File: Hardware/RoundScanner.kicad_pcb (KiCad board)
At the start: 2 copper layers, 50.1 x 50.1 mm, 87 parts, among them J1 I2C Debug, J2 Screen, J3 SPI Debug, SW1 TRIGGER, SW2 RESET, U1 OPA2376xxD, U2 ADS1256IDBT, U3 LM285D-2.5, U4 AMS1117-3.3, U5 TLC59208FIPWR, U6 ESP32-DevKitC, Y1 8MHz

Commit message: Version 0.1
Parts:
- removed B1: Button, Connector_JST:JST_SH_BM04B-SRSS-TB_1x04-1MP_P1.00mm_Vertical
- removed CH1: Power, Connector_JST:JST_XH_B2B-XH-A_1x02_P2.50mm_Vertical
- removed D12: WS2812B, LED_SMD:LED_WS2812B_PLCC4_5.0x5.0mm_P3.2mm
- removed FB1: FerriteBead, Resistor_SMD:R_0805_2012Metric_Pad1.20x1.40mm_HandSolder
- removed J3: SPI Debug, Connector_JST:JST_XH_B4B-XH-A_1x04_P2.50mm_Vertical
- removed JP1: SolderJumper_2_Open, Jumper:SolderJumper-2_P1.3mm_Open_TrianglePad1.0x1.5mm
- removed JP2, JP3: SolderJumper_3_Open, Jumper:SolderJumper-3_P2.0mm_Open_TrianglePad1.0x1.5mm_NumberLabels
- removed R13: 0, Resistor_SMD:R_0805_2012Metric_Pad1.20x1.40mm_HandSolder
- removed R14, R15: 100, Resistor_SMD:R_0805_2012Metric_Pad1.20x1.40mm_HandSolder
- removed R19: 10k, Resistor_SMD:R_0805_2012Metric_Pad1.20x1.40mm_HandSolder
- removed SW1: TRIGGER, Button_Switch_THT:SW_PUSH_6mm
- removed SW2: RESET, Button_Switch_THT:SW_PUSH_6mm
- removed TP0: Test_GND, TestPoint:TestPoint_Pad_D1.5mm
- removed TP1: Test_5V, TestPoint:TestPoint_Pad_D1.5mm
- removed TP52: TestPoint_Small, TestPoint:TestPoint_Pad_D1.0mm
- removed Y1: 8MHz, Crystal:Crystal_SMD_3225-4Pin_3.2x2.5mm_HandSoldering
- added L1: INDUCTOR, Inductor_SMD:L_0603_1608Metric, F.Cu at (106.0, 119.1)
- added Q1: BSS138DW-7-F, BSS138DW-7-F-A:Diodes_Inc._-_BSS138DW-7-F-A, F.Cu at (102.7, 90.7)
- added REF**: MountingHole_2.5mm, MountingHole:MountingHole_2.5mm, F.Cu at (99.7, 117.7)
- added REF**: MountingHole_2.5mm, MountingHole:MountingHole_2.5mm, F.Cu at (71.5, 97.4)
- added REF**: MountingHole_2.5mm, MountingHole:MountingHole_2.5mm, F.Cu at (89.4, 124.6)
- added U7: AP7312-1833W6-7, AP7312-1833W6-7:AP7312-1833W6-7, F.Cu at (106.3, 101.7)
- C1, C13, C16, C17, C18, C2, C3, C4, C5: footprint Capacitor_SMD:C_0805_2012Metric_Pad1.18x1.45mm_HandSolder -> Capacitor_SMD:C_0603_1608Metric_Pad1.08x0.95mm_HandSolder
- C10: value 18p -> 0.1uF; footprint Capacitor_SMD:C_0805_2012Metric_Pad1.18x1.45mm_HandSolder -> Capacitor_SMD:C_0603_1608Metric_Pad1.08x0.95mm_HandSolder
- C11: value 10u -> 2.2uF; footprint Capacitor_SMD:C_0805_2012Metric_Pad1.18x1.45mm_HandSolder -> Capacitor_SMD:C_0603_1608Metric_Pad1.08x0.95mm_HandSolder
- C12: value 22u -> 2.2uF; footprint Capacitor_SMD:C_0805_2012Metric_Pad1.18x1.45mm_HandSolder -> Capacitor_SMD:C_0603_1608Metric_Pad1.08x0.95mm_HandSolder
- C14: value 100n -> 10uF; footprint Capacitor_SMD:C_0805_2012Metric_Pad1.18x1.45mm_HandSolder -> Capacitor_SMD:C_0603_1608Metric_Pad1.08x0.95mm_HandSolder
- C15: value 10 -> 10uF; footprint Capacitor_SMD:C_0805_2012Metric_Pad1.18x1.45mm_HandSolder -> Capacitor_SMD:C_0603_1608Metric_Pad1.08x0.95mm_HandSolder
- C19: value 104 -> 10uF; footprint Capacitor_SMD:C_0805_2012Metric_Pad1.18x1.45mm_HandSolder -> Capacitor_SMD:C_0603_1608Metric_Pad1.08x0.95mm_HandSolder
- C20: value 104 -> 0.1uF; footprint Capacitor_SMD:C_0805_2012Metric_Pad1.18x1.45mm_HandSolder -> Capacitor_SMD:C_0603_1608Metric_Pad1.08x0.95mm_HandSolder
- C6: value 22u -> 1uF; footprint Capacitor_SMD:C_0805_2012Metric_Pad1.18x1.45mm_HandSolder -> Capacitor_SMD:C_0603_1608Metric_Pad1.08x0.95mm_HandSolder
- C7: value 100n -> 0.1uF; footprint Capacitor_SMD:C_0805_2012Metric_Pad1.18x1.45mm_HandSolder -> Capacitor_SMD:C_0603_1608Metric_Pad1.08x0.95mm_HandSolder
- C8: value 100p -> 0.1uF; footprint Capacitor_SMD:C_0805_2012Metric_Pad1.18x1.45mm_HandSolder -> Capacitor_SMD:C_0603_1608Metric_Pad1.08x0.95mm_HandSolder
- C9: value 18p -> 470pF; footprint Capacitor_SMD:C_0805_2012Metric_Pad1.18x1.45mm_HandSolder -> Capacitor_SMD:C_0603_1608Metric_Pad1.08x0.95mm_HandSolder
- D2: value WS2812B -> POWER LED; footprint LED_SMD:LED_WS2812B_PLCC4_5.0x5.0mm_P3.2mm -> LED_SMD:LED_0805_2012Metric_Pad1.15x1.40mm_HandSolder
- D3: value POWER LED -> EAHC2835WD6; footprint LED_SMD:LED_0805_2012Metric_Pad1.15x1.40mm_HandSolder -> Everlight-EAHC2835WD6:Everlight-EAHC2835WD6-MFG
- J2: value Screen -> I2C; footprint Connector_JST:JST_XH_S8B-XH-A_1x08_P2.50mm_Horizontal -> Connector_JST:JST_SH_SM04B-SRSS-TB_1x04-1MP_P1.00mm_Horizontal
- R1, R2, R20, R21, R22, R23, R24, R25, R26, R27, R28, R29, R3, R30, R31, R32, R4, R7, R8: footprint Resistor_SMD:R_0805_2012Metric_Pad1.20x1.40mm_HandSolder -> Resistor_SMD:R_0603_1608Metric_Pad0.98x0.95mm_HandSolder
- R10, R12, R9: value 100 -> 10k; footprint Resistor_SMD:R_0805_2012Metric_Pad1.20x1.40mm_HandSolder -> Resistor_SMD:R_0603_1608Metric_Pad0.98x0.95mm_HandSolder
- R11: value 0 -> 10k; footprint Resistor_SMD:R_0805_2012Metric_Pad1.20x1.40mm_HandSolder -> Resistor_SMD:R_0603_1608Metric_Pad0.98x0.95mm_HandSolder
- R16: value 170 -> 150; footprint Resistor_SMD:R_0805_2012Metric_Pad1.20x1.40mm_HandSolder -> Resistor_SMD:R_0603_1608Metric_Pad0.98x0.95mm_HandSolder
- R17: value 150 -> 316k; footprint Resistor_SMD:R_0805_2012Metric_Pad1.20x1.40mm_HandSolder -> Resistor_SMD:R_0603_1608Metric_Pad0.98x0.95mm_HandSolder
- R18: value 10k -> 100k; footprint Resistor_SMD:R_0805_2012Metric_Pad1.20x1.40mm_HandSolder -> Resistor_SMD:R_0603_1608Metric_Pad0.98x0.95mm_HandSolder
- R5, R6: value 49.9 -> 51; footprint Resistor_SMD:R_0805_2012Metric_Pad1.20x1.40mm_HandSolder -> Resistor_SMD:R_0603_1608Metric_Pad0.98x0.95mm_HandSolder
- U1: footprint eec:Texas_Instruments-OPA2376AID-Level_A -> OPA2376AID:SOIC127P599X175-8N
- U2: value ADS1256IDBT -> NAU7802SGI; footprint ADS1256IDBT:SOP65P780X200-28N -> Nuvoton-NAU7802SGI:Nuvoton-NAU7802SGI
- U4: value AMS1117-3.3 -> TPS61023DRLR; footprint Package_TO_SOT_SMD:SOT-223-3_TabPin2 -> TPS61023DRLR:Texas_Instruments_-_TPS61023DRLR
- U6: value ESP32-DevKitC -> AS7341-DLGT; footprint ESP32:ESP32-DevKitC -> AS7341-DLGT:PSON80P310X200X110-8N
- moved C17 139.8 mm to (89.8, 128.9), turned to -90 degrees
- moved C16 134.9 mm to (91.4, 128.9), turned to 90 degrees
- moved C15 125.5 mm to (109.3, 101.8), turned to -90 degrees
- moved C12 122.9 mm to (108.6, 116.8), turned to -90 degrees
- moved C11 121.0 mm to (103.1, 116.8), turned to 90 degrees
- moved C14 119.0 mm to (111.0, 101.8), turned to -90 degrees
- moved R20 116.4 mm to (112.1, 107.4), turned to 90 degrees
- moved C13 115.1 mm to (110.4, 107.4), turned to -90 degrees
- moved U4 113.5 mm to (106.0, 116.8)
- moved D3 113.5 mm to (96.4, 104.6), turned to 180 degrees
- moved U3 111.2 mm to (105.8, 108.5)
- moved R17 99.2 mm to (107.6, 113.4), turned to 180 degrees
- moved J2 92.1 mm to (99.6, 123.6), turned to 45 degrees
- moved R18 86.7 mm to (104.1, 113.4), turned to 180 degrees
- moved D2 77.5 mm to (96.1, 127.6), turned to 135 degrees
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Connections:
- C10 pad 1: Net-(C10-Pad1) -> GND
- C10 pad 2: GND -> Net-(C10-Pad2)
- C11 pad 1: +5VD -> +3V3
- C12 pad 1: +5V -> Net-(C12-Pad1)
- C14 pad 1: +5V -> GND
- C14 pad 2: GND -> +3V3
- C15 pad 1: +5VD -> GND
- C15 pad 2: GND -> +3V3
- C19 pad 1: +5VD -> GND
- C19 pad 2: GND -> +1V8
- C20 pad 1: +5VD -> GND
- C20 pad 2: GND -> +1V8
- C6 pad 1: Net-(C6-Pad1) -> GND
- C7 pad 1: Net-(C6-Pad1) -> GND
- C8 pad 1: Net-(C6-Pad1) -> Net-(C8-Pad1)
- C8 pad 2: Net-(C6-Pad2) -> Net-(C8-Pad2)
- C9 pad 1: GND -> Net-(C9-Pad1)
- D2 pad 1: +5VD -> GND
- D2 pad 2: Net-(D12-Pad4) -> Net-(D2-Pad2)
- D3 pad 1: GND -> +3V3
- J1 pad 1: /ADC/ADC RESET -> GND
- J2 pad 1: +3V3 -> GND
- J2 pad 2: GND -> +3V3
- J2 pad 3: MOSI-Screen -> SDA
- J2 pad 4: CLK-Screen -> SCL
- R10 pad 1: V-MOSI -> +3V3
- R10 pad 2: Net-(R10-Pad2) -> SDA
- R11 pad 1: V-MISO -> +3V3
- R11 pad 2: Net-(R11-Pad2) -> SCL
- R12 pad 1: CS1 -> SDA
- R12 pad 2: Net-(R12-Pad2) -> +3V3
- R16 pad 1: LED -> +3V3
- R16 pad 2: Net-(D2-Pad4) -> Net-(D2-Pad2)
- R17 pad 1: +3V3 -> Net-(C12-Pad1)
- R17 pad 2: Net-(D3-Pad2) -> Net-(R17-Pad2)
- R18 pad 1: +5VD -> Net-(R17-Pad2)
- R18 pad 2: MCU Reset -> GND
- R20 pad 1: +5V -> Net-(C12-Pad1)
- R5 pad 1: +2V5 -> /ADC/AIN+
- R5 pad 2: Net-(C6-Pad1) -> Net-(C8-Pad1)
- R6 pad 1: GND -> /ADC/AIN-
- R6 pad 2: Net-(C6-Pad2) -> Net-(C8-Pad2)
- R7 pad 1: Net-(R14-Pad2) -> +1V8
- R7 pad 2: +3V3 -> /MCU + IO/SCL_2v
- R8 pad 1: +3V3 -> +1V8
- R8 pad 2: Net-(R15-Pad2) -> /MCU + IO/SDA_2v
- R9 pad 1: V-CLK -> +3V3
- R9 pad 2: Net-(R9-Pad2) -> SCL
- U1 pad 8: +5V -> +3V3
- U2 pad 1: +5V -> Net-(C6-Pad2)
- U2 pad 13: unconnected-(U2-Pad13) -> SCL
- U2 pad 14: Net-(R15-Pad2) -> SDA
- U2 pad 15: Net-(R14-Pad2) -> +3V3
- U2 pad 16: +3V3 -> unconnected-(U2-Pad16)
- U2 pad 2: GND -> Net-(C8-Pad2)
- U2 pad 3: Net-(C6-Pad2) -> Net-(C8-Pad1)
- U2 pad 4: Net-(C6-Pad1) -> Net-(C9-Pad2)
- U2 pad 5: GND -> Net-(C9-Pad1)
- U2 pad 6: /ADC/AIN+ -> Net-(C10-Pad2)
- U2 pad 7: /ADC/AIN- -> GND
- U2 pad 8: unconnected-(U2-Pad8) -> GND
- U2 pad 9: unconnected-(U2-Pad9) -> GND
- U4 pad 1: GND -> Net-(R17-Pad2)
- U4 pad 2: +3V3 -> GND
- U4 pad 3: +5VD -> +3V3
- U6 pad 1: unconnected-(U6-Pad1) -> +1V8
- U6 pad 2: unconnected-(U6-Pad2) -> /MCU + IO/SCL_2v
- U6 pad 3: unconnected-(U6-Pad3) -> GND
- U6 pad 4: unconnected-(U6-Pad4) -> Net-(D3-Pad2)
- U6 pad 7: /LED/LED RESET -> unconnected-(U6-Pad7)
- U6 pad 8: Trigger -> /MCU + IO/SDA_2v
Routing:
- net GND: track 48.9 -> 202.8 mm, vias 2 -> 9
- net SDA: track 0.00 -> 109.8 mm, vias 0 -> 5
- net SCL: track 0.00 -> 104.5 mm, vias 0 -> 4
- net +3V3: track 74.7 -> 178.9 mm, vias 2 -> 8
- net /ADC/AIN-: track 56.8 -> 5.69 mm, vias 2 -> 0
- net Net-(R14-Pad2): track 48.8 -> 0.00 mm
- net +1V8: track 0.00 -> 32.1 mm, vias 0 -> 2
- net Net-(C9-Pad2): track 30.9 -> 2.10 mm
- net /MCU + IO/SDA_2v: track 0.00 -> 26.6 mm, vias 0 -> 4
- net /ADC/AIN+: track 33.6 -> 7.20 mm
- net Net-(R15-Pad2): track 22.3 -> 0.00 mm, vias 2 -> 0
- net +2V5: track 20.4 -> 39.9 mm
- net /MCU + IO/SCL_2v: track 0.00 -> 16.6 mm, vias 0 -> 2
- net Net-(R27-Pad1): track 25.0 -> 9.54 mm
- net Net-(C8-Pad1): track 0.00 -> 14.2 mm
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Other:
- board size 50.1 x 50.1 mm -> 49.1 x 49.1 mm

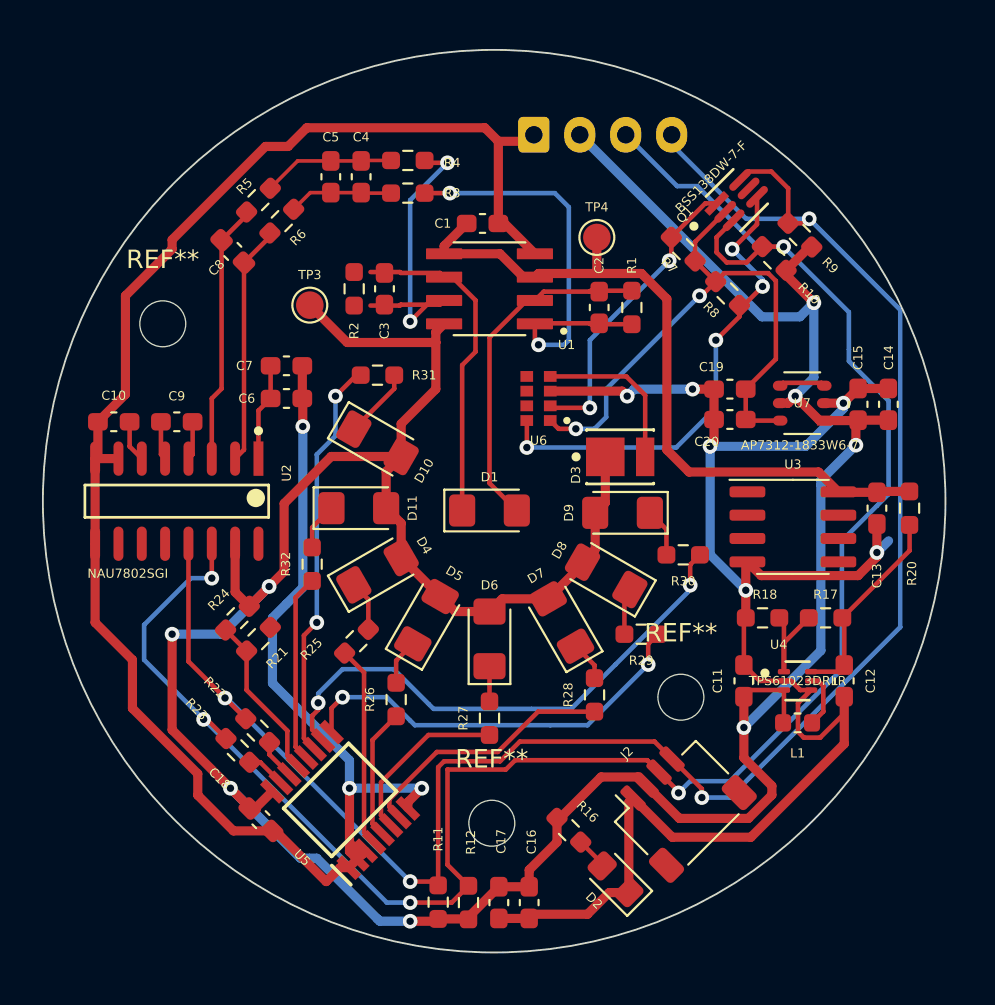
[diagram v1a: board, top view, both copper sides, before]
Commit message: Added gnd zones
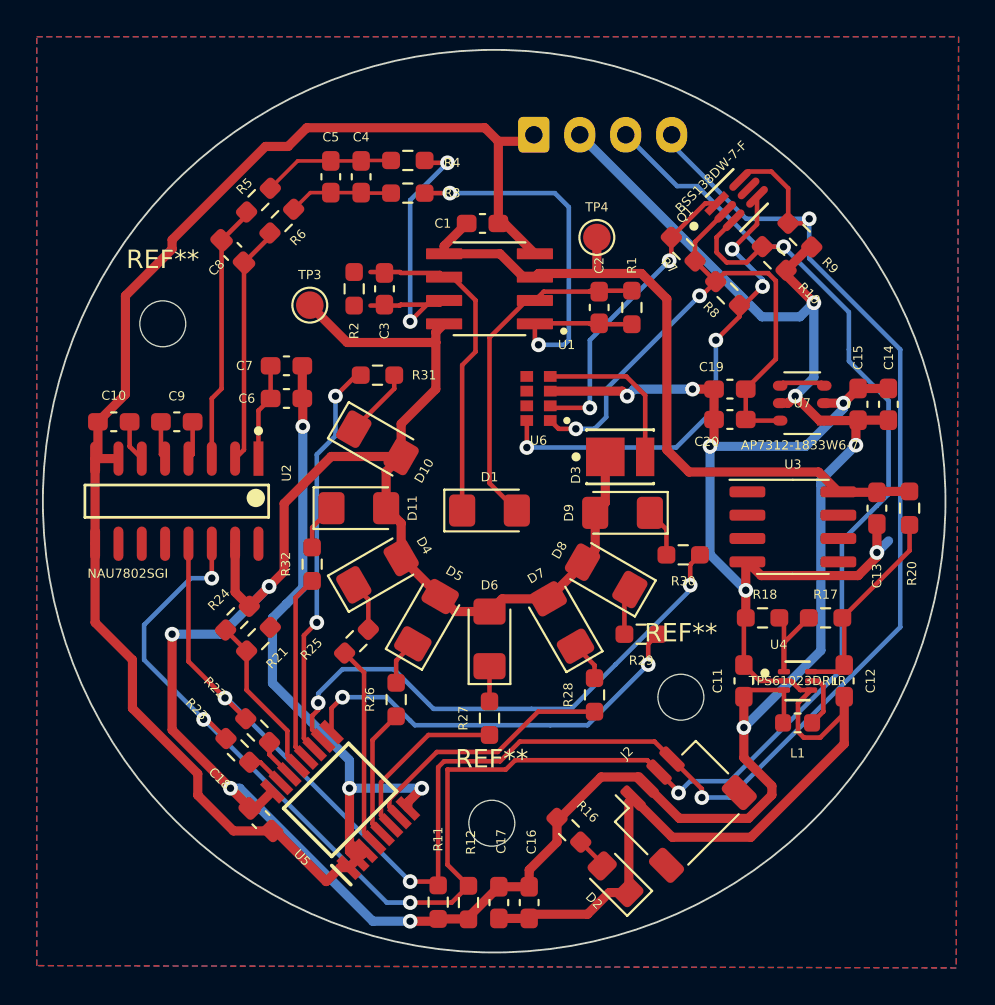
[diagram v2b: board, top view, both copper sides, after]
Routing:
- added copper zone on B.Cu, net GND
- added copper zone on F.Cu, net GND
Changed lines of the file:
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@@
     (pts (xy 38.608 177.8) (xy 38.608 102.87))
     (height 32.385)
-    (gr_text "74.9300 mm" (at 69.843 140.335 90) (layer "User.1")
+    (gr_text "74.9300 mm" (at 70.393 140.335 90) (layer "User.1")
       (effects (font (size 0.5 0.5) (thickness 0.1)))
     )
@@
     (pts (xy 38.935112 178.562) (xy 38.862 108.204))
     (height 26.519362)
-    (gr_text "70.3580 mm" (at 66.567903 143.354248 -89.94046153) (layer "User.1")
+    (gr_text "70.3580 mm" (at 66.017904 143.35482 -89.94046153) (layer "User.1")
       (effects (font (size 0.5 0.5) (thickness 0.1)))
     )
@@
     (pts (xy 40.767 178.562) (xy 40.64 135.001))
     (height 20.929362)
-    (gr_text "43.5612 mm" (at 62.782768 156.717129 -89.83295738) (layer "User.1")
+    (gr_text "43.5612 mm" (at 62.23277 156.718733 -89.83295738) (layer "User.1")
       (effects (font (size 0.5 0.5) (thickness 0.1)))
     )
@@
   (segment (start 106.934 100.33) (end 105.918 101.346) (width 0.5) (layer "B.Cu") (net 11))
   (segment (start 106.934 96.266) (end 106.172 97.028) (width 0.5) (layer "B.Cu") (net 11))
-  (segment (start 78.994 126.492) (end 79.502 126.492) (width 0.5) (layer "B.Cu") (net 11))
   (segment (start 106.934 96.266) (end 106.934 100.33) (width 0.5) (layer "B.Cu") (net 11))
   (segment (start 103.124 119.38) (end 107.315 115.189) (width 0.5) (layer "B.Cu") (net 11))
   (segment (start 104.1 97.028) (end 94.194 87.122) (width 0.5) (layer "B.Cu") (net 11))
+  (segment (start 82.931 129.921) (end 84.963 129.921) (width 0.5) (layer "B.Cu") (net 11))
   (segment (start 74.692376 114.3) (end 72.009 114.3) (width 0.5) (layer "B.Cu") (net 11))
   (segment (start 106.172 97.028) (end 104.1 97.028) (width 0.5) (layer "B.Cu") (net 11))
-  (segment (start 75.184 122.682) (end 78.994 126.492) (width 0.5) (layer "B.Cu") (net 11))
+  (segment (start 75.184 122.682) (end 75.692 122.682) (width 0.5) (layer "B.Cu") (net 11))
   (segment (start 77.287688 111.704688) (end 74.692376 114.3) (width 0.5) (layer "B.Cu") (net 11))
+  (segment (start 75.692 122.682) (end 82.931 129.921) (width 0.5) (layer "B.Cu") (net 11))
   (segment (start 107.315 106.172) (end 107.315 105.918) (width 0.5) (layer "B.Cu") (net 11))
-  (segment (start 79.883 126.492) (end 83.185 129.794) (width 0.5) (layer "B.Cu") (net 11))
-  (segment (start 79.502 126.492) (end 79.883 126.492) (width 0.5) (layer "B.Cu") (net 11))
-  (segment (start 83.185 129.794) (end 83.312 129.921) (width 0.5) (layer "B.Cu") (net 11))
-  (segment (start 83.312 129.921) (end 84.963 129.921) (width 0.5) (layer "B.Cu") (net 11))
   (segment (start 82.687235 112.405198) (end 81.896787 111.61475) (width 0.25) (layer "F.Cu") (net 12))
   (segment (start 82.687235 114.035765) (end 82.687235 112.405198) (width 0.25) (layer "F.Cu") (net 12))
@@
   (via (at 106.68 91.694) (size 0.8) (drill 0.4) (layers "F.Cu" "B.Cu") (net 39))
   (via (at 84.963 127.762) (size 0.8) (drill 0.4) (layers "F.Cu" "B.Cu") (net 39))
+  (segment (start 102.362 123.19) (end 100.838 123.19) (width 0.25) (layer "B.Cu") (net 39))
   (segment (start 103.251 91.694) (end 99.194 87.637) (width 0.25) (layer "B.Cu") (net 39))
+  (segment (start 106.68 91.694) (end 106.68 93.853) (width 0.25) (layer "B.Cu") (net 39))
   (segment (start 74.888289 117.770711) (end 74.971711 117.770711) (width 0.25) (layer "B.Cu") (net 39))
   (segment (start 111.633 113.919) (end 102.362 123.19) (width 0.25) (layer "B.Cu") (net 39))
+  (segment (start 106.68 93.853) (end 111.633 98.806) (width 0.25) (layer "B.Cu") (net 39))
   (segment (start 99.194 87.637) (end 99.194 87.122) (width 0.25) (layer "B.Cu") (net 39))
   (segment (start 106.68 91.694) (end 103.251 91.694) (width 0.25) (layer "B.Cu") (net 39))
-  (segment (start 102.362 123.19) (end 100.838 123.19) (width 0.25) (layer "B.Cu") (net 39))
   (segment (start 74.971711 117.770711) (end 84.963 127.762) (width 0.25) (layer "B.Cu") (net 39))
-  (segment (start 106.68 91.694) (end 111.633 96.647) (width 0.25) (layer "B.Cu") (net 39))
-  (segment (start 111.633 96.647) (end 111.633 113.919) (width 0.25) (layer "B.Cu") (net 39))
+  (segment (start 111.633 98.806) (end 111.633 113.919) (width 0.25) (layer "B.Cu") (net 39))
   (segment (start 95.414216 126.910216) (end 95.414216 126.783216) (width 0.25) (layer "F.Cu") (net 40))
   (segment (start 95.414216 126.783216) (end 94.244235 125.613235) (width 0.25) (layer "F.Cu") (net 40))
@@
   (segment (start 105.2545 100.621499) (end 105.099 100.776999) (width 0.25) (layer "F.Cu") (net 53))
   (segment (start 107.499 100.776999) (end 107.3435 100.621499) (width 0.25) (layer "F.Cu") (net 53))
+  (zone (net 1) (net_name "GND") (layers F&B.Cu) (hatch edge 0.508)
+    (connect_pads (clearance 0.8))
+    (min_thickness 0.254) (filled_areas_thickness no)
+    (fill yes (thermal_gap 0.508) (thermal_bridge_width 0.508) (smoothing fillet))
+    (polygon
+      (pts
+        (xy 114.681 132.461)
+        (xy 64.643 132.334)
+        (xy 64.643 81.788)
+        (xy 114.808 81.788)
+      )
+    )
+  )
+  (zone (net 0) (net_name "") (layers F&B.Cu) (hatch edge 0.508)
+    (connect_pads (clearance 0))
+    (min_thickness 0.254)
+    (keepout (tracks not_allowed) (vias not_allowed) (pads not_allowed ) (copperpour allowed) (footprints allowed))
+    (fill (thermal_gap 0.508) (thermal_bridge_width 0.508))
+    (polygon
+      (pts
+        (xy 93.853 110.617)
+        (xy 85.598 110.617)
+        (xy 85.598 87.757)
+        (xy 93.853 87.757)
+      )
+    )
+  )
 )

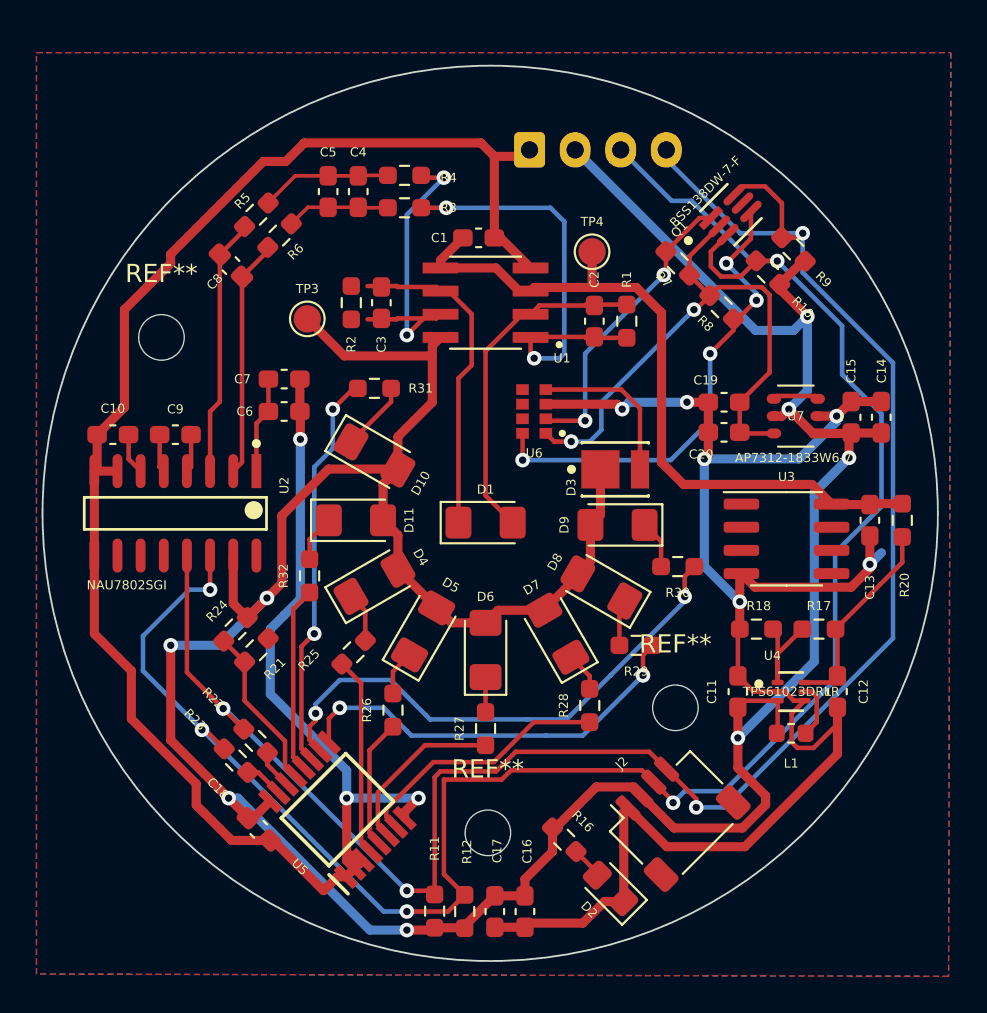
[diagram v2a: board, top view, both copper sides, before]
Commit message: Udated mounting hole layout
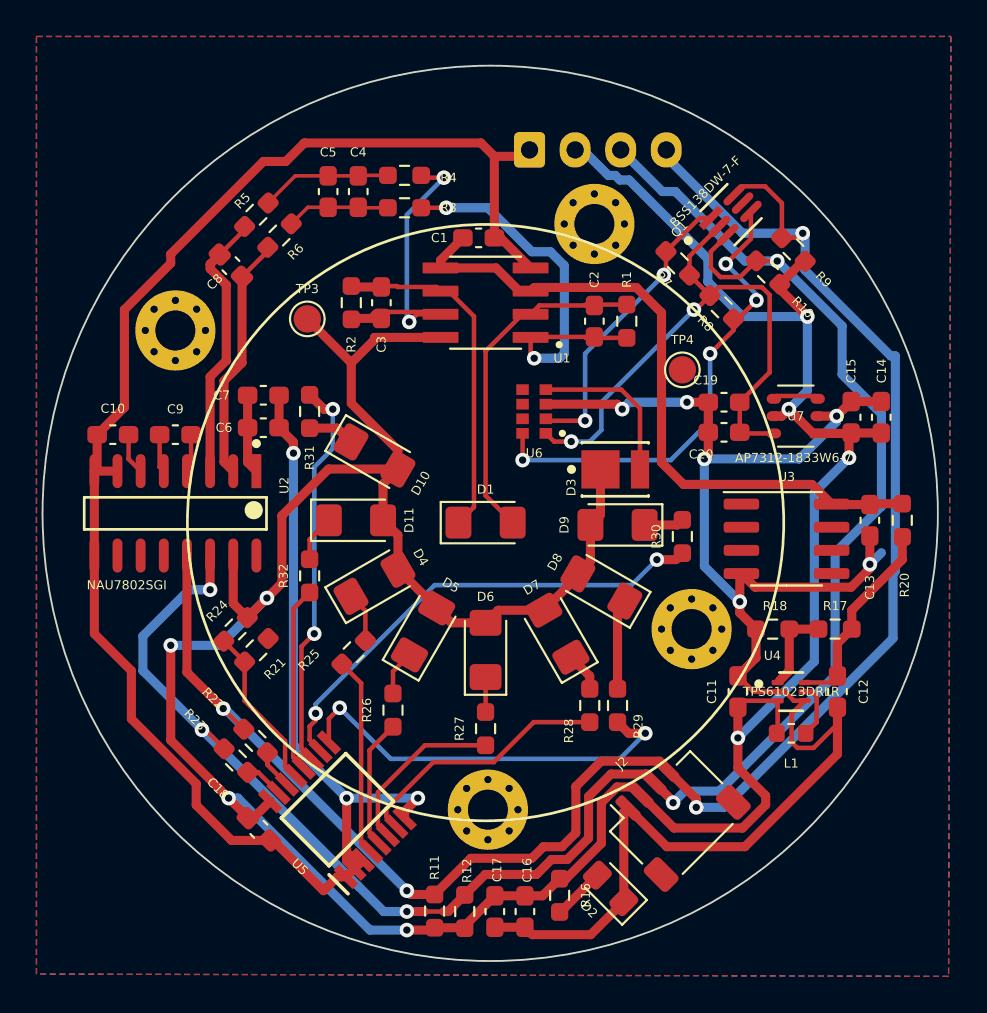
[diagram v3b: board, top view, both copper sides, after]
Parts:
- removed the REF** at (71.5, 97.4)
- added REF**: MountingHole_2.2mm_M2_Pad_Via, MountingHole:MountingHole_2.2mm_M2_Pad_Via, F.Cu at (95.2, 91.2)
- added REF**: MountingHole_2.2mm_M2_Pad_Via, MountingHole:MountingHole_2.2mm_M2_Pad_Via, F.Cu at (89.4, 123.3)
- REF** (x2): value MountingHole_2.5mm -> MountingHole_2.2mm_M2_Pad_Via; footprint MountingHole:MountingHole_2.5mm -> MountingHole:MountingHole_2.2mm_M2_Pad_Via
- moved REF** 32.5 mm to (72.3, 97.0)
- moved TP4 8.15 mm to (100.1, 99.2)
- moved REF** 4.41 mm to (100.6, 113.4)
- moved R31 3.78 mm to (79.6, 101.5), turned to -90 degrees
- moved R29 3.45 mm to (96.5, 117.6), turned to 90 degrees
- moved R16 3.06 mm to (93.3, 128.0), turned to -90 degrees
- moved R30 1.67 mm to (100.1, 108.3), turned to 90 degrees
- moved C7 1.45 mm to (77.1, 100.6)
- moved C6 1.45 mm to (77.1, 102.4)
- moved R17 0.89 mm to (108.5, 113.4)
- moved R18 0.89 mm to (105.0, 113.4)
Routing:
- net SDA: track 109.8 -> 123.1 mm
- net Net-(R30-Pad1): track 29.4 -> 26.5 mm
- net Net-(D8-Pad1): track 2.55 -> 5.40 mm
- net SCL: track 104.5 -> 101.9 mm
- net +2V5: track 39.9 -> 38.0 mm
- net Net-(R17-Pad2): track 6.52 -> 4.66 mm
- net Net-(C3-Pad1): track 18.1 -> 19.9 mm
- net Net-(C12-Pad1): track 11.1 -> 12.6 mm
- net Net-(C2-Pad2): track 23.2 -> 21.8 mm
- net Net-(D10-Pad1): track 3.85 -> 2.58 mm
- net Net-(D2-Pad2): track 1.78 -> 3.03 mm
- net Net-(C6-Pad2): track 5.32 -> 4.36 mm
- net GND: track 202.8 -> 202.0 mm
- net Net-(C8-Pad1): track 14.2 -> 14.9 mm
- net Net-(C3-Pad2): track 17.2 -> 17.9 mm
